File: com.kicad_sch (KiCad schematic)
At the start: 0 parts

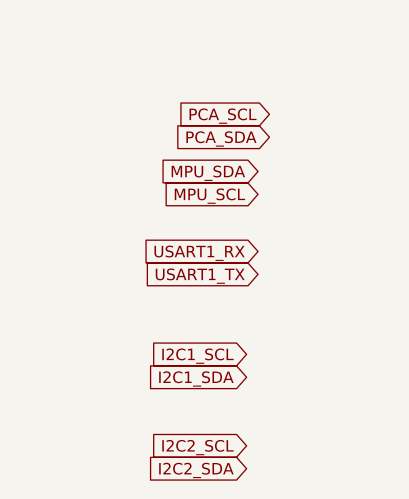
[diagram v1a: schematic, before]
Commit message: gpio expander added comm finished
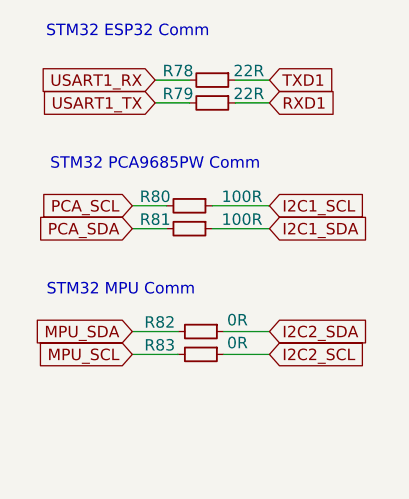
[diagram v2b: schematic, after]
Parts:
- added R78, R79: 22R, Resistor_SMD:R_0805_2012Metric, symbol Device:R_Small
- added R80, R81: 100R, Resistor_SMD:R_0805_2012Metric, symbol Device:R_Small
- added R82, R83: 0R, Resistor_SMD:R_0805_2012Metric, symbol Device:R_Small
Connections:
- net I2C1_SCL: now also R80.1
- net I2C1_SDA: now also R81.1
- net I2C2_SCL: now also R83.1
- net I2C2_SDA: now also R82.1
- net MPU_SCL: now also R83.2
- net MPU_SDA: now also R82.2
- net PCA_SCL: now also R80.2
- net PCA_SDA: now also R81.2
- net USART1_RX: now also R78.2
- net USART1_TX: now also R79.2
- new net RXD1: R79.1
- new net TXD1: R78.1
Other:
- note added: "STM32 ESP32 Comm"
- note added: "STM32 MPU Comm"
- note added: "STM32 PCA9685PW Comm"

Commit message: schematic finished
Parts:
- renumbered R78 to R19, R79 to R20, R80 to R21, R81 to R22, R82 to R23, R83 to R24
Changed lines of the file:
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@@
 		(on_board yes)
 		(dnp no)
-		(property "Reference" "R78"
+		(property "Reference" "R19"
 			(at 30.48 20.574 90)
 			(effects
@@
 			(project "controllerForVehicle"
 				(path "/f177fb06-71dc-4865-9331-a828b12c2bf7/fc85c3d3-062f-408a-ac80-59caebdc7296"
-					(reference "R78")
+					(reference "R19")
 					(unit 1)
 				)
@@
 		(on_board yes)
 		(dnp no)
-		(property "Reference" "R80"
+		(property "Reference" "R21"
 			(at 27.94 34.544 90)
 			(effects
@@
 			(project "controllerForVehicle"
 				(path "/f177fb06-71dc-4865-9331-a828b12c2bf7/fc85c3d3-062f-408a-ac80-59caebdc7296"
-					(reference "R80")
+					(reference "R21")
 					(unit 1)
 				)
@@
 		(on_board yes)
 		(dnp no)
-		(property "Reference" "R79"
+		(property "Reference" "R20"
 			(at 30.48 23.114 90)
 			(effects
@@
 			(project "controllerForVehicle"
 				(path "/f177fb06-71dc-4865-9331-a828b12c2bf7/fc85c3d3-062f-408a-ac80-59caebdc7296"
-					(reference "R79")
+					(reference "R20")
 					(unit 1)
 				)
@@
 		(on_board yes)
 		(dnp no)
-		(property "Reference" "R83"
+		(property "Reference" "R24"
 			(at 28.448 51.054 90)
 			(effects
@@
 			(project "controllerForVehicle"
 				(path "/f177fb06-71dc-4865-9331-a828b12c2bf7/fc85c3d3-062f-408a-ac80-59caebdc7296"
-					(reference "R83")
+					(reference "R24")
 					(unit 1)
 				)
@@
 		(on_board yes)
 		(dnp no)
-		(property "Reference" "R81"
+		(property "Reference" "R22"
 			(at 27.94 37.084 90)
 			(effects
@@
 			(project "controllerForVehicle"
 				(path "/f177fb06-71dc-4865-9331-a828b12c2bf7/fc85c3d3-062f-408a-ac80-59caebdc7296"
-					(reference "R81")
+					(reference "R22")
 					(unit 1)
 				)
@@
 		(on_board yes)
 		(dnp no)
-		(property "Reference" "R82"
+		(property "Reference" "R23"
 			(at 28.448 48.514 90)
 			(effects
@@
 			(project "controllerForVehicle"
 				(path "/f177fb06-71dc-4865-9331-a828b12c2bf7/fc85c3d3-062f-408a-ac80-59caebdc7296"
-					(reference "R82")
-					(unit 1)
-				)
+					(reference "R23")
+					(unit 1)
+				)

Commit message: silinecek
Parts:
- renumbered R19 to R22, R20 to R23, R21 to R24, R22 to R25, R23 to R26, R24 to R27
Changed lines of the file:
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@@
 		(on_board yes)
 		(dnp no)
-		(property "Reference" "R19"
+		(property "Reference" "R22"
 			(at 30.48 20.574 90)
 			(effects
@@
 			(project "controllerForVehicle"
 				(path "/f177fb06-71dc-4865-9331-a828b12c2bf7/fc85c3d3-062f-408a-ac80-59caebdc7296"
-					(reference "R19")
+					(reference "R22")
 					(unit 1)
 				)
@@
 		(on_board yes)
 		(dnp no)
-		(property "Reference" "R21"
+		(property "Reference" "R24"
 			(at 27.94 34.544 90)
 			(effects
@@
 			(project "controllerForVehicle"
 				(path "/f177fb06-71dc-4865-9331-a828b12c2bf7/fc85c3d3-062f-408a-ac80-59caebdc7296"
-					(reference "R21")
+					(reference "R24")
 					(unit 1)
 				)
@@
 		(on_board yes)
 		(dnp no)
-		(property "Reference" "R20"
+		(property "Reference" "R23"
 			(at 30.48 23.114 90)
 			(effects
@@
 			(project "controllerForVehicle"
 				(path "/f177fb06-71dc-4865-9331-a828b12c2bf7/fc85c3d3-062f-408a-ac80-59caebdc7296"
-					(reference "R20")
+					(reference "R23")
 					(unit 1)
 				)
@@
 		(on_board yes)
 		(dnp no)
-		(property "Reference" "R24"
+		(property "Reference" "R27"
 			(at 28.448 51.054 90)
 			(effects
@@
 			(project "controllerForVehicle"
 				(path "/f177fb06-71dc-4865-9331-a828b12c2bf7/fc85c3d3-062f-408a-ac80-59caebdc7296"
-					(reference "R24")
+					(reference "R27")
 					(unit 1)
 				)
@@
 		(on_board yes)
 		(dnp no)
-		(property "Reference" "R22"
+		(property "Reference" "R25"
 			(at 27.94 37.084 90)
 			(effects
@@
 			(project "controllerForVehicle"
 				(path "/f177fb06-71dc-4865-9331-a828b12c2bf7/fc85c3d3-062f-408a-ac80-59caebdc7296"
-					(reference "R22")
+					(reference "R25")
 					(unit 1)
 				)
@@
 		(on_board yes)
 		(dnp no)
-		(property "Reference" "R23"
+		(property "Reference" "R26"
 			(at 28.448 48.514 90)
 			(effects
@@
 			(project "controllerForVehicle"
 				(path "/f177fb06-71dc-4865-9331-a828b12c2bf7/fc85c3d3-062f-408a-ac80-59caebdc7296"
-					(reference "R23")
-					(unit 1)
-				)
+					(reference "R26")
+					(unit 1)
+				)
